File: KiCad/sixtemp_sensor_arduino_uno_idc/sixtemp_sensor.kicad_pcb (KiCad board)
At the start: 2 copper layers, 53.3 x 68.6 mm, 39 parts, among them J10 debug, J12 Sig_conn, J123456 Led_EN, J13 RB_Conn, J14 GND_GRN_Conn, J31 1-Wire, J32 1-Wire, J33 1-Wire, J34 1-Wire, J35 1-Wire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

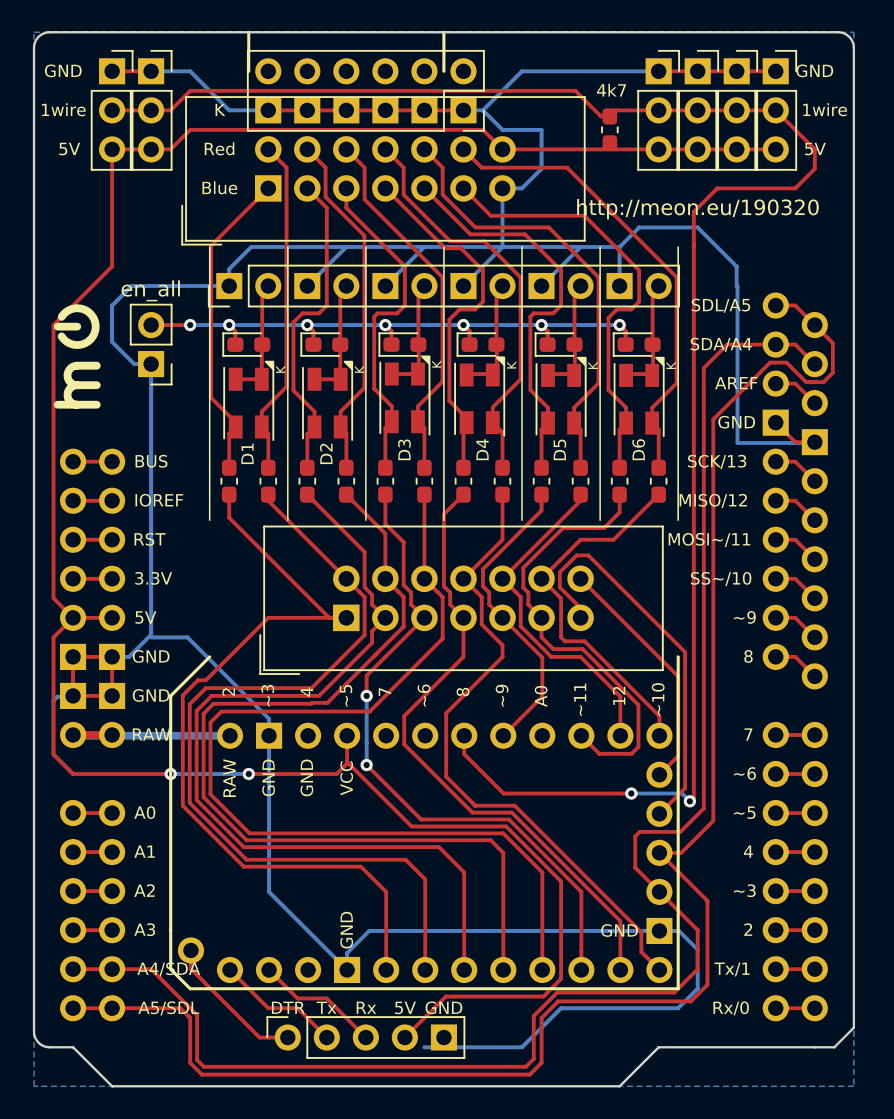
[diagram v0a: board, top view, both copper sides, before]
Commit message: add seventh led diode & holes to use all of the pins
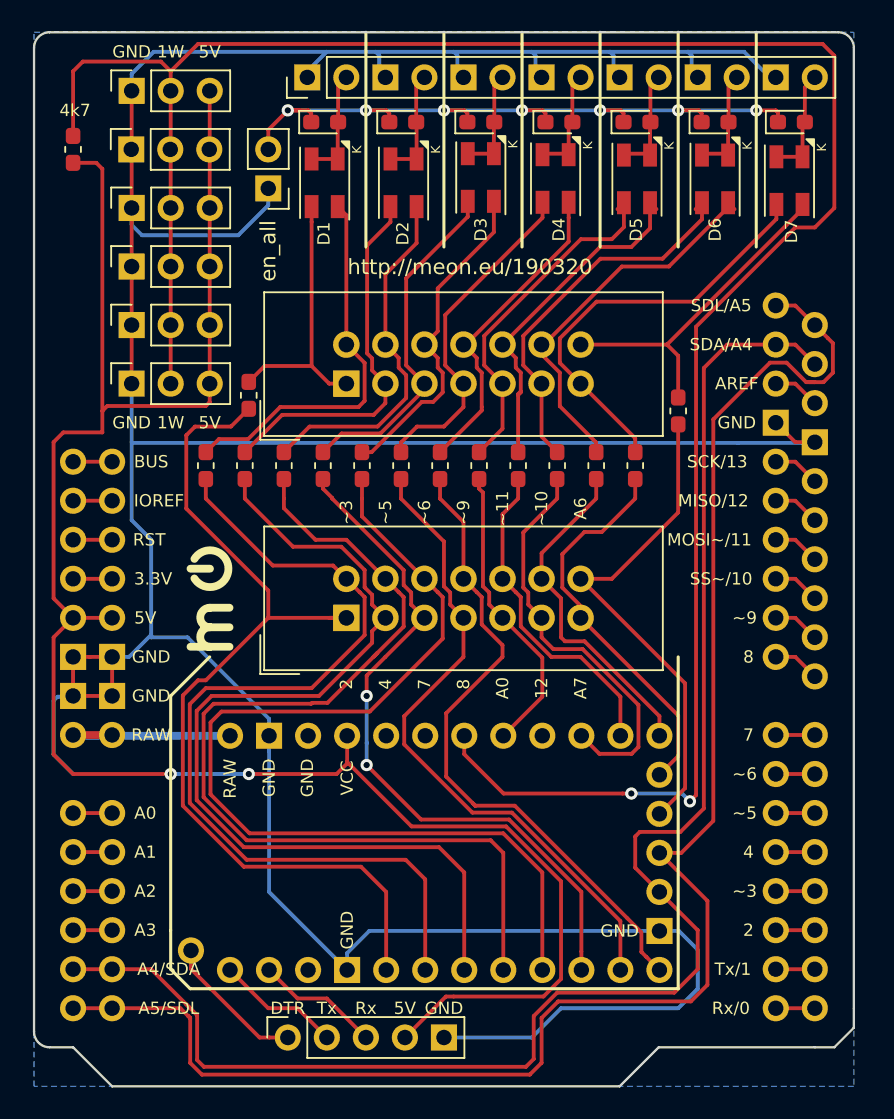
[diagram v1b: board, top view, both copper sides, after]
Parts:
- removed J14: GND_GRN_Conn, Connector_PinSocket_2.54mm:PinSocket_2x06_P2.54mm_Vertical
- added D7: LED_Dual_AACC, LED_SMD:LED_WL_SBTW_PLCC4_2.4x2.4mm_P1.7mm, F.Cu at (115.2, 42.7)
- added D79: D, Diode_SMD:D_0603_1608Metric_Pad1.05x0.95mm_HandSolder, F.Cu at (115.3, 38.9)
- added R71: 1k, Resistor_SMD:R_0603_1608Metric_Pad1.05x0.95mm_HandSolder, F.Cu at (108.0, 57.7)
- added R72: 1k, Resistor_SMD:R_0603_1608Metric_Pad1.05x0.95mm_HandSolder, F.Cu at (105.2, 61.2)
- J123456: footprint Connector_PinHeader_2.54mm:PinHeader_1x12_P2.54mm_Vertical -> Connector_PinHeader_2.54mm:PinHeader_1x14_P2.54mm_Vertical
- moved J31 42.8 mm to (72.4, 44.5), turned to 90 degrees
- moved J32 41.4 mm to (72.4, 48.3), turned to 90 degrees
- moved J33 40.4 mm to (72.4, 52.1), turned to 90 degrees
- moved J34 39.9 mm to (72.4, 55.9), turned to 90 degrees
- moved R101 34.9 mm to (68.6, 40.6)
- moved D59 15.3 mm to (105.3, 38.9)
- moved D69 15.3 mm to (110.3, 38.9)
- moved D19 15.3 mm to (84.9, 38.9)
- moved D29 15.3 mm to (90.0, 38.9)
- moved D39 15.3 mm to (95.1, 38.9)
- moved D49 15.3 mm to (100.2, 38.9)
- moved D5 15.2 mm to (105.3, 42.6)
- moved D6 15.2 mm to (110.3, 42.6)
- moved D3 15.2 mm to (95.1, 42.5)
- moved D2 15.2 mm to (90.1, 42.8)
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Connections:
- J12 pad 13: A6 -> A7
- J12 pad 14: A7 -> A6
- J13 pad 13: GND -> D7_Blue
- J13 pad 14: +5V -> D7_Red
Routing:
- net 1wire: track 114.7 -> 146.7 mm
- net D7_Blue: track 0.00 -> 28.0 mm
- net D7_Red: track 0.00 -> 22.1 mm
- net +5V: track 146.0 -> 131.0 mm
- net GND: track 261.8 -> 248.1 mm
- net en_all_led: track 39.1 -> 49.5 mm
- net A7: track 15.9 -> 25.5 mm
- net D2: track 52.4 -> 60.5 mm
- net EN_D7: track 0.00 -> 7.20 mm
- net A6: track 26.0 -> 32.7 mm
- net D5_Red: track 29.0 -> 22.9 mm
- net D4_Red: track 26.7 -> 20.8 mm
- net D6_Red: track 30.5 -> 25.2 mm
- net D3~~: track 54.7 -> 59.7 mm
- net D4: track 56.9 -> 61.4 mm
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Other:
- board text added: "1W"
- board text added: "A6"
- board text added: "A7"
- board text removed: "1wire"
- board text removed: "Blue"
- board text removed: "K"
- board text removed: "Red"

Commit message: add 2x i2c pullups
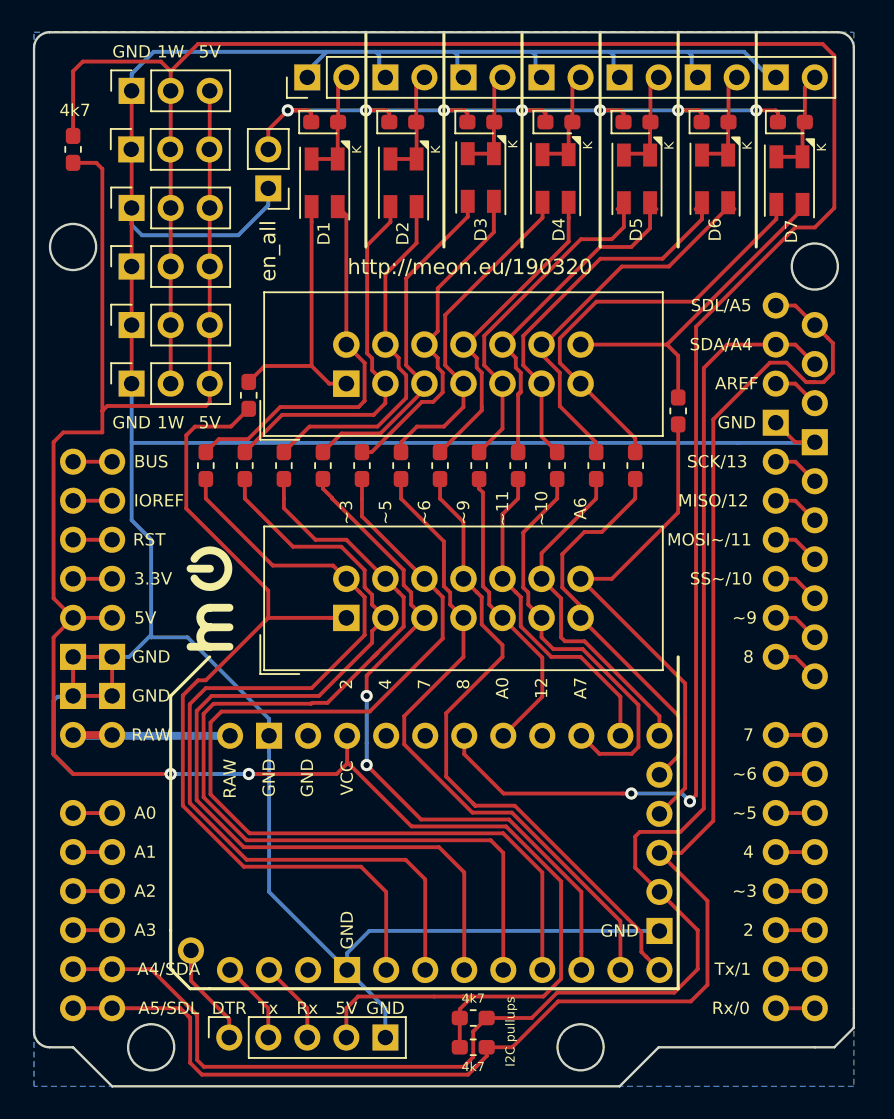
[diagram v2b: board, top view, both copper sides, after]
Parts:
- added R81: 4k7, Resistor_SMD:R_0603_1608Metric_Pad1.05x0.95mm_HandSolder, F.Cu at (94.6, 97.2)
- added R82: 4k7, Resistor_SMD:R_0603_1608Metric_Pad1.05x0.95mm_HandSolder, F.Cu at (94.6, 99.1)
- moved J10 3.81 mm to (78.7, 98.4)
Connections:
- U1 pad 17: (no net) -> Net-(U1-Pad17)
- U1 pad 25: (no net) -> Net-(U1-Pad25)
- U1 pad 26: (no net) -> Net-(U1-Pad26)
- U1 pad 29: (no net) -> Net-(U1-Pad29)
- U1 pad 92: (no net) -> Net-(U1-Pad92)
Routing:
- net GND: track 248.1 -> 230.2 mm
- net +5V: track 131.0 -> 139.7 mm
- net Rx: track 8.12 -> 5.43 mm
- net Tx: track 8.12 -> 5.43 mm
- net DTR: track 9.35 -> 6.70 mm
- net SCL: track 106.6 -> 105.2 mm
- net SDA: track 102.2 -> 101.5 mm
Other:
- outline, holes or cut-outs redrawn
- board text added: "I2C pullups"

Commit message: update labels, different layout
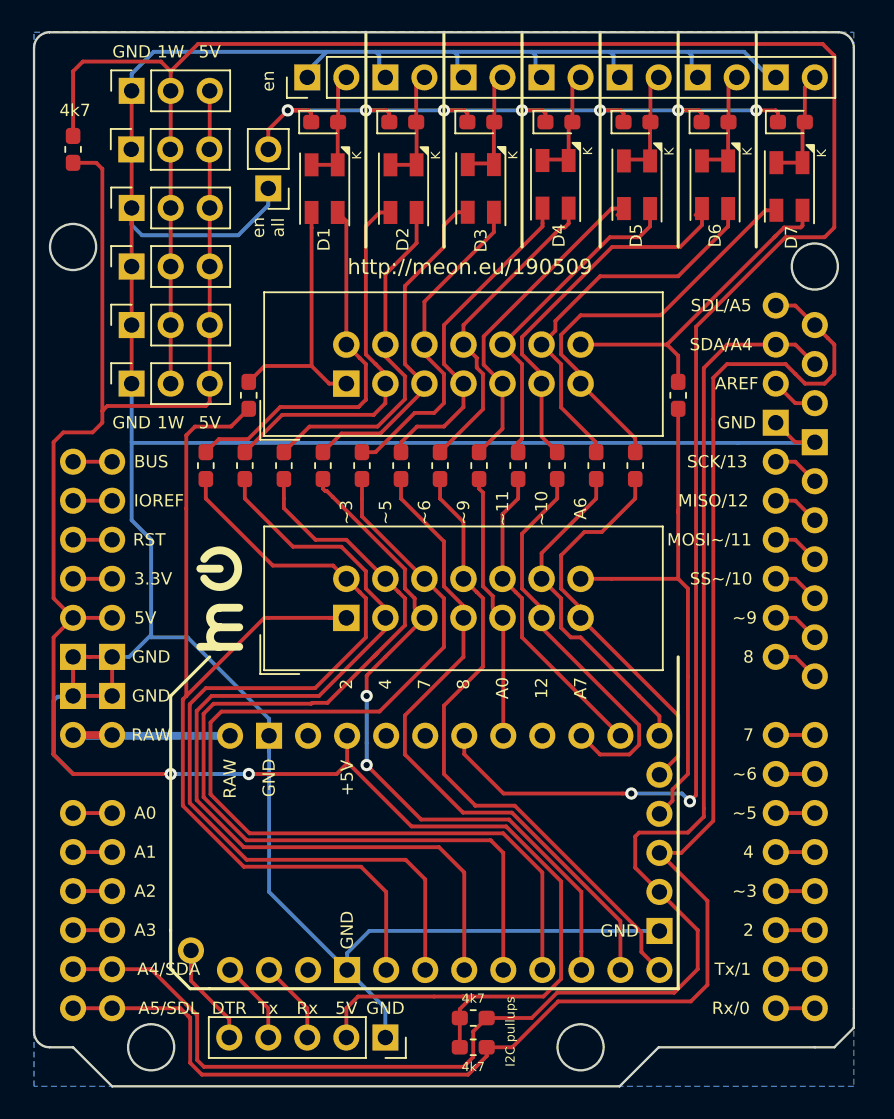
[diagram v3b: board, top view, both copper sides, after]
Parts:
- moved J10 10.2 mm to (88.9, 98.4), turned to 270 degrees
- moved R71 1.02 mm to (108.0, 56.6)
- moved D3 0.71 mm to (95.1, 43.2)
- moved D1 0.38 mm to (84.9, 43.2)
- moved D2 0.38 mm to (90.1, 43.2)
- moved D4 0.38 mm to (100.0, 42.9)
- moved D5 0.38 mm to (105.3, 42.9)
- moved D6 0.38 mm to (110.3, 42.9)
- moved D7 0.38 mm to (115.2, 43.1)
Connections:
- J10 pad 1: DTR -> GND
- J10 pad 2: Tx -> +5V
- J10 pad 4: +5V -> Tx
- J10 pad 5: GND -> DTR
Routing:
- net D2: track 60.5 -> 63.2 mm
- net A0: track 19.5 -> 17.4 mm
- net SCL: track 105.2 -> 106.6 mm
- net D5_Red: track 22.9 -> 21.6 mm
- net A6: track 32.7 -> 33.9 mm
- net D9~~: track 42.6 -> 41.5 mm
- net 11_MISO~~: track 21.4 -> 20.3 mm
- net D5_Blue: track 22.9 -> 21.8 mm
- net 12_MISO: track 27.0 -> 25.9 mm
- net A7: track 25.5 -> 26.3 mm
- net 1wire: track 146.7 -> 147.5 mm
- net EN_D3: track 6.90 -> 7.61 mm
- net D7_Blue: track 28.0 -> 27.3 mm
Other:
- board text added: "en"
- board text added: "en all"
- board text added: "http://meon.eu/190509"
- board text removed: "http://meon.eu/190320"

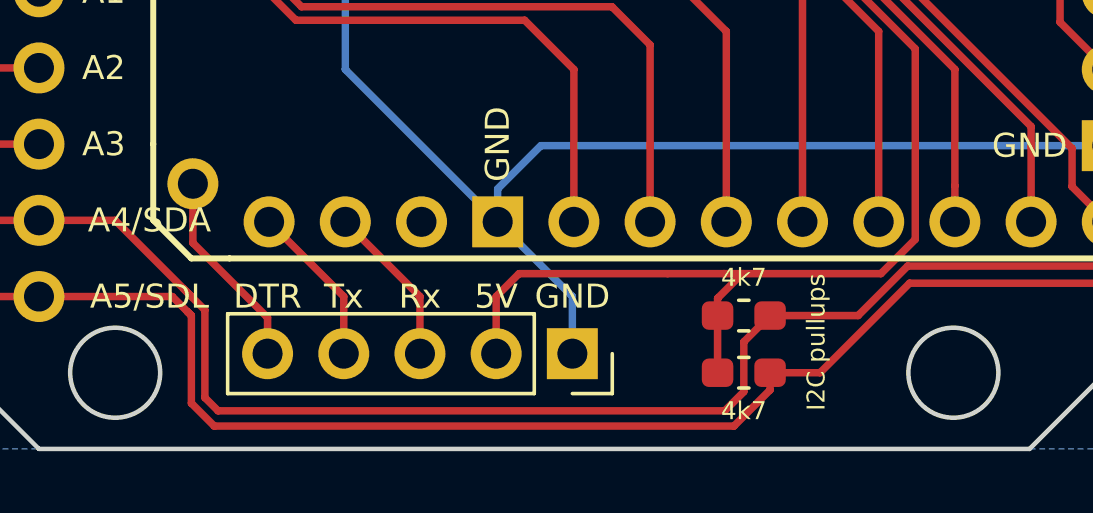
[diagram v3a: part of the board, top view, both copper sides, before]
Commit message: 5->6 pin debug connector
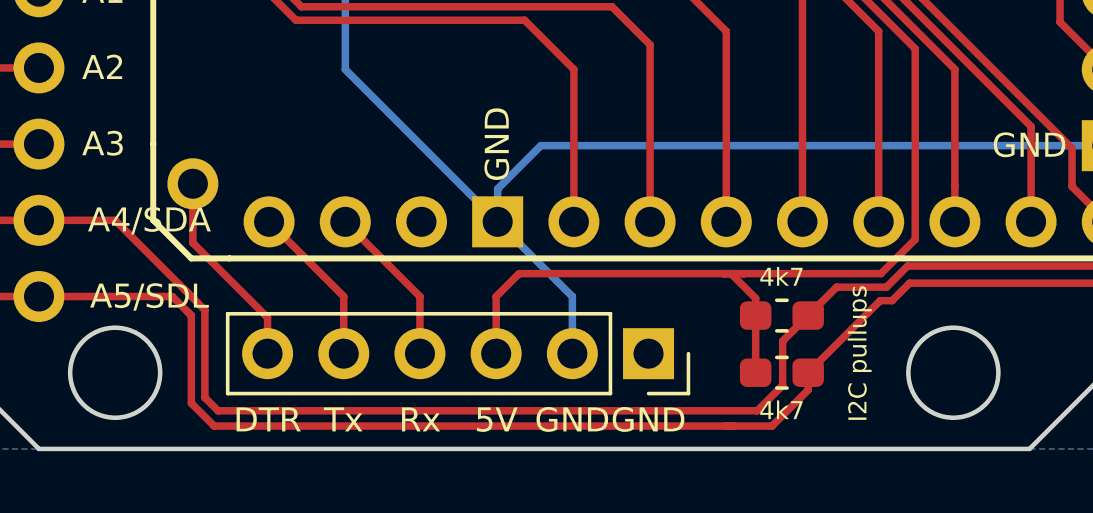
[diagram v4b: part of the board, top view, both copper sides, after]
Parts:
- J10: footprint Connector_PinSocket_2.54mm:PinSocket_1x05_P2.54mm_Vertical -> Connector_PinSocket_2.54mm:PinSocket_1x06_P2.54mm_Vertical
- moved J10 2.54 mm to (91.4, 98.4)
- moved R81 1.27 mm to (95.9, 97.2)
- moved R82 1.27 mm to (95.9, 99.1)
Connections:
- J10 pad 2: +5V -> GND
- J10 pad 3: Rx -> +5V
- J10 pad 4: Tx -> Rx
- J10 pad 5: DTR -> Tx

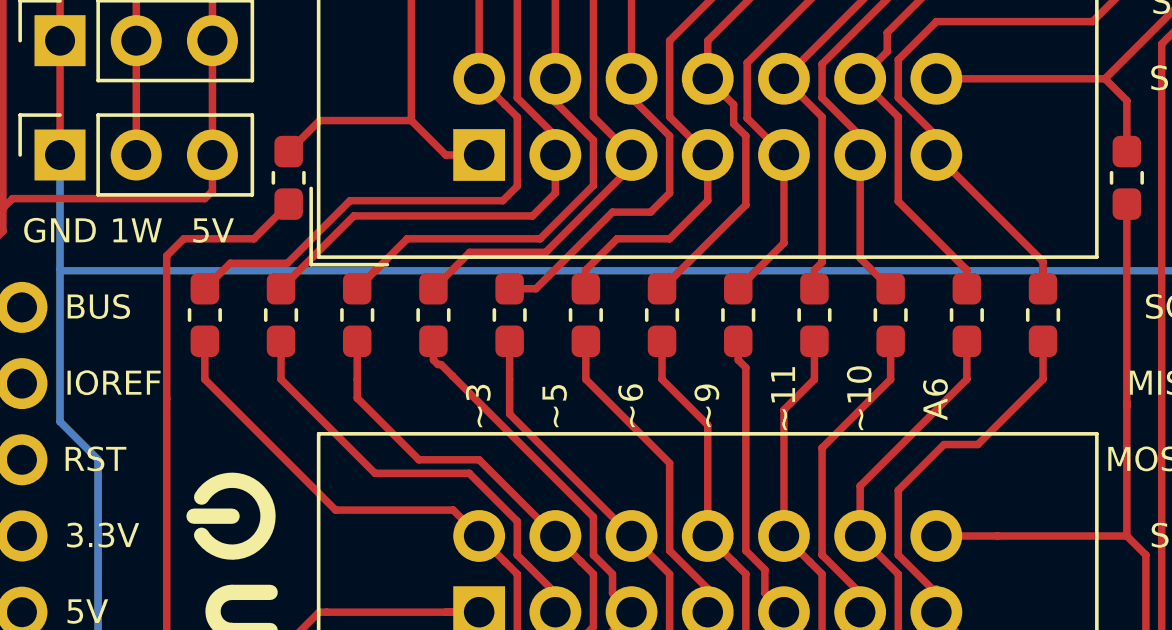
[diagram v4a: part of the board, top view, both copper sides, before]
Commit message: label resistors for red led
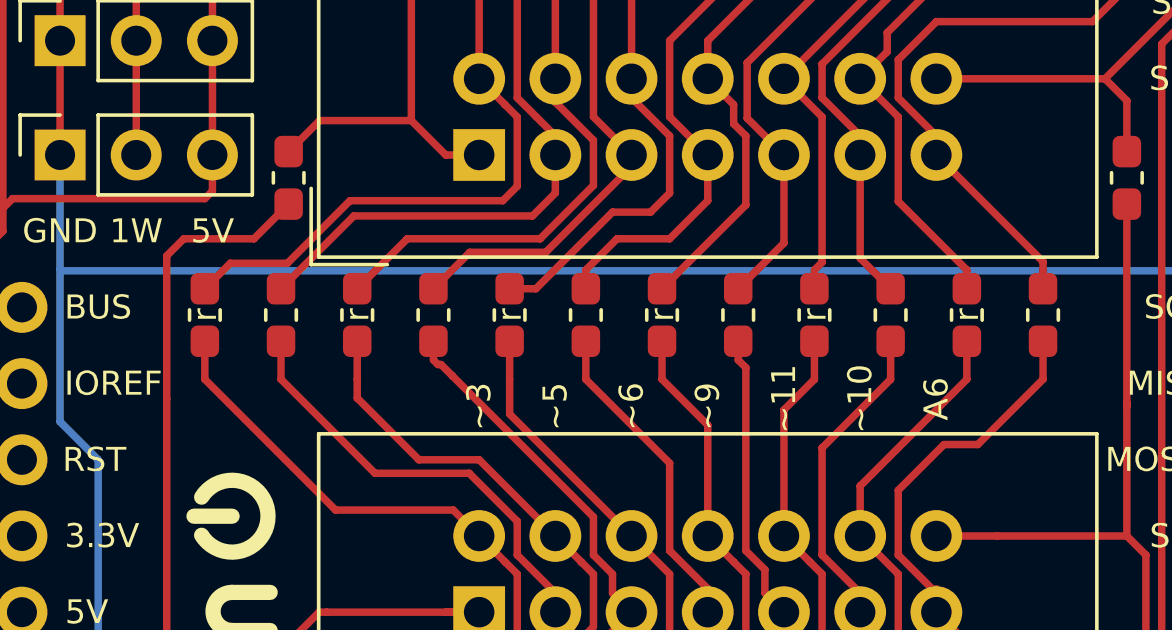
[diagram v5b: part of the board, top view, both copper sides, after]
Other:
- board text added: "r"
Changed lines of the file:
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@@
   (general
     (thickness 1.6)
-    (drawings 79)
+    (drawings 85)
     (tracks 640)
     (zones 0)
@@
     )
   )
+  (gr_text r (at 102.616 61.214 90) (layer F.SilkS)
+    (effects (font (size 0.8 0.8) (thickness 0.125)))
+  )
+  (gr_text r (at 97.536 61.214 90) (layer F.SilkS)
+    (effects (font (size 0.8 0.8) (thickness 0.125)))
+  )
+  (gr_text r (at 92.456 61.214 90) (layer F.SilkS)
+    (effects (font (size 0.8 0.8) (thickness 0.125)))
+  )
+  (gr_text r (at 87.376 61.214 90) (layer F.SilkS)
+    (effects (font (size 0.8 0.8) (thickness 0.125)))
+  )
+  (gr_text r (at 82.296 61.214 90) (layer F.SilkS)
+    (effects (font (size 0.8 0.8) (thickness 0.125)))
+  )
+  (gr_text r (at 77.216 61.214 90) (layer F.SilkS)
+    (effects (font (size 0.8 0.8) (thickness 0.125)))
+  )
   (gr_text GND (at 91.44 100.6475) (layer F.SilkS)
